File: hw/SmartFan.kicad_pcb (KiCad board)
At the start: 2 copper layers, 111 x 62.5 mm, 40 parts, among them J1 Barrel_Jack, J2 JTAG_SWD, J3 FAN_CONN, Q1 MMBT2222A-TP, Q2 MMBT2222A-TP, Q3 MMBT2222A-TP, Q4 MMBT2222A-7-F, Q5 MMBT2222A-7-F, Q6 MMBT2222A-7-F, U1 L7805CV, U2 LTV-816S-TA1, U3 LTV-816S-TA1, U4 LTV-816S-TA1

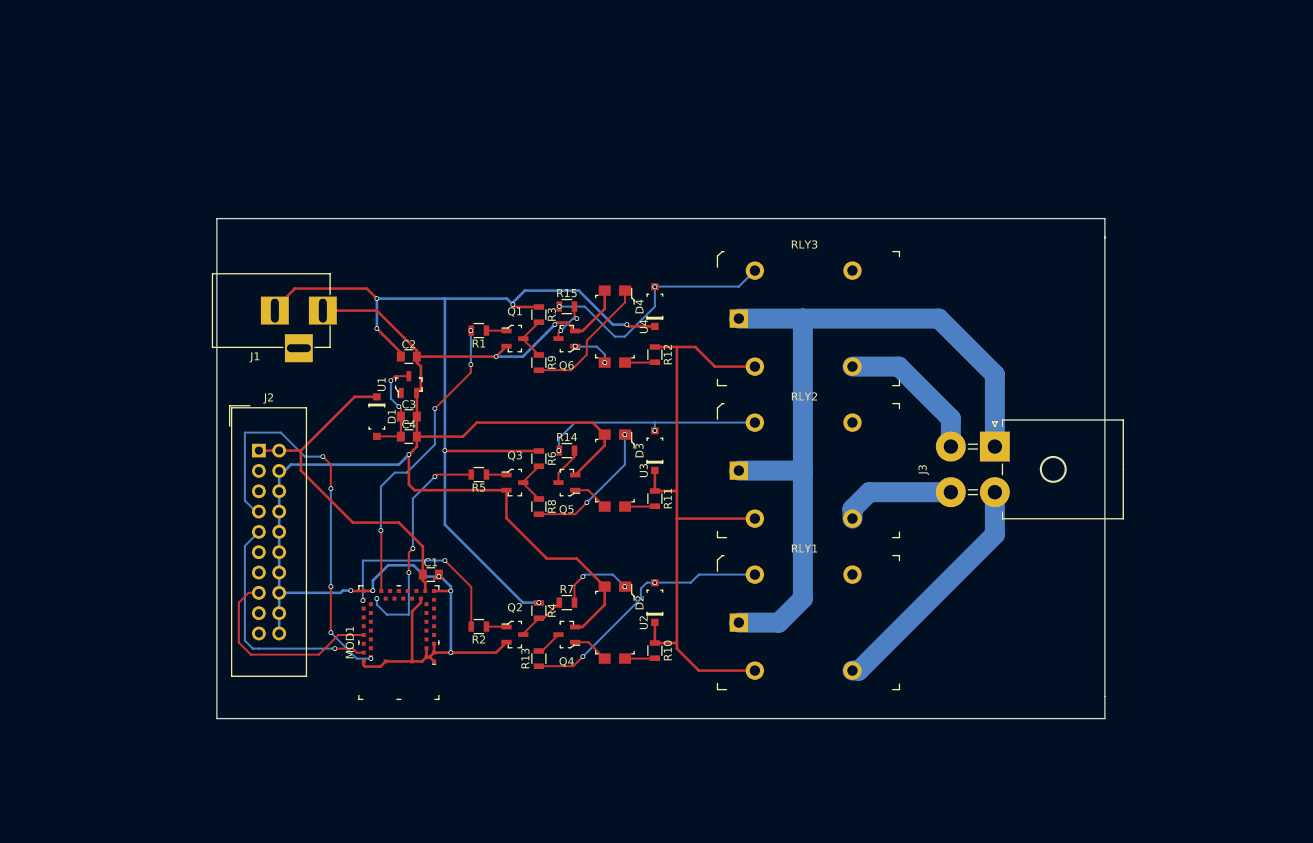
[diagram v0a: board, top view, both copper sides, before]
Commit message: Updated schematics and PCB
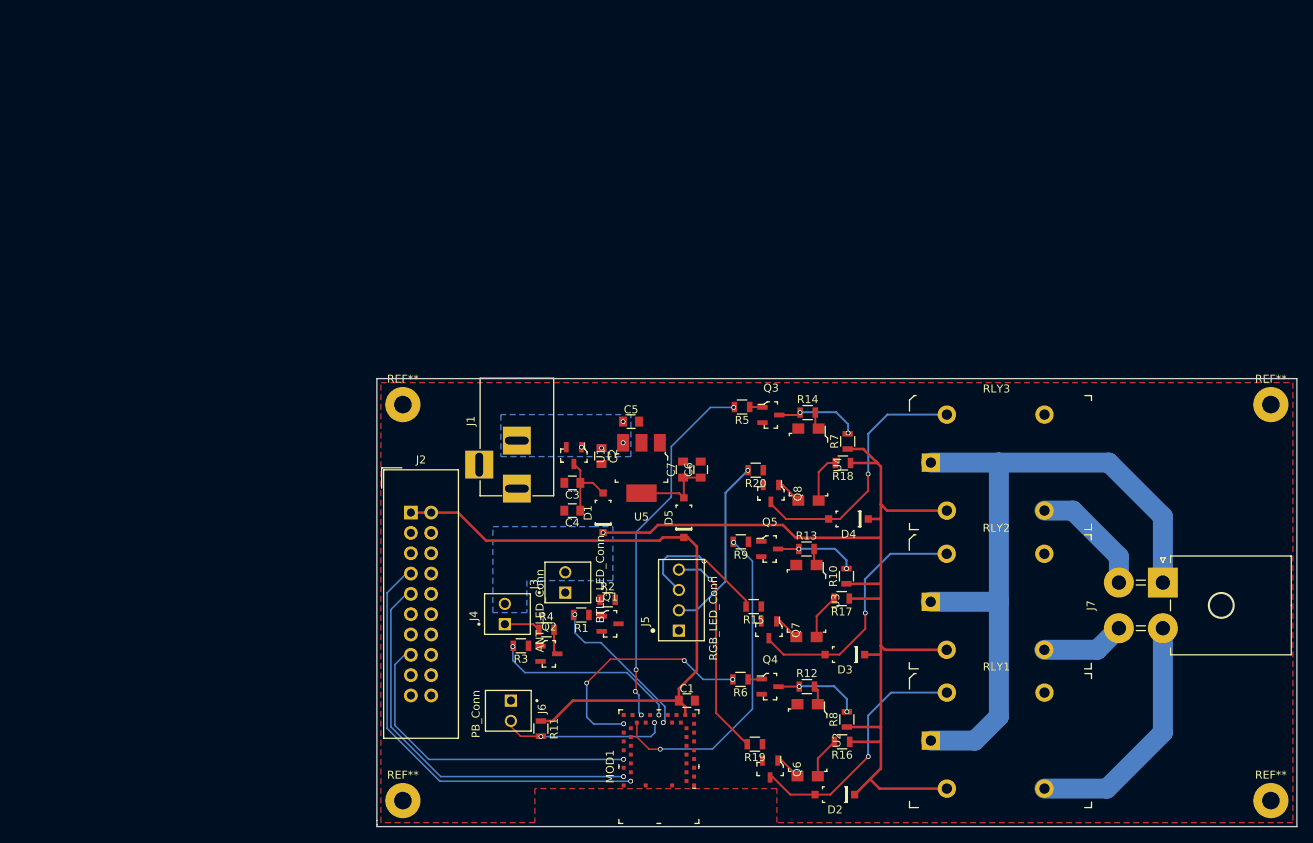
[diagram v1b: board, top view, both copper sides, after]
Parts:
- added C5: 1uF, Capacitors_SMD:C_0805, F.Cu at (143.8, 85.4)
- added C6: 1uF, Capacitors_SMD:C_0805, F.Cu at (152.5, 91.4)
- added C7: 0.1uF, Capacitors_SMD:C_0805, F.Cu at (150.3, 91.4)
- added D5: MBR0540T1G, digikey-footprints:SOD-123, F.Cu at (150.4, 97.4)
- added J4: ANT_LED_Conn, 640456-2:TE_640456-2, F.Cu at (128.0, 110.7)
- added J5: RGB_LED_Conn, 640456-4:TE_640456-4, F.Cu at (149.8, 111.5)
- added J6: PB_Conn, 640456-2:TE_640456-2, F.Cu at (128.8, 120.2)
- added J7: FAN_CONN, Connectors_Molex:Molex_MegaFit_2x02x5.70mm_Angled, F.Cu at (210.2, 105.5)
- added Q7: MMBT2222A-7-F, digikey-footprints:SOT-23-3, F.Cu at (161.0, 111.4)
- added Q8: MMBT2222A-7-F, digikey-footprints:SOT-23-3, F.Cu at (161.2, 94.3)
- added R16: 1k, Resistors_SMD:R_0805, F.Cu at (170.2, 125.4)
- added R17: 1k, Resistors_SMD:R_0805, F.Cu at (170.1, 107.5)
- added R18: 1k, Resistors_SMD:R_0805, F.Cu at (170.2, 90.5)
- added R19: 330, Resistors_SMD:R_0805, F.Cu at (159.2, 125.7)
- added R20: 330, Resistors_SMD:R_0805, F.Cu at (159.3, 91.5)
- added REF**: MountingHole_2.2mm_M2_Pad, Mounting_Holes:MountingHole_2.2mm_M2_Pad, F.Cu at (115.2, 83.2)
- added REF**: MountingHole_2.2mm_M2_Pad, Mounting_Holes:MountingHole_2.2mm_M2_Pad, F.Cu at (115.2, 132.8)
- added REF**: MountingHole_2.2mm_M2_Pad, Mounting_Holes:MountingHole_2.2mm_M2_Pad, F.Cu at (223.8, 132.8)
- added REF**: MountingHole_2.2mm_M2_Pad, Mounting_Holes:MountingHole_2.2mm_M2_Pad, F.Cu at (223.8, 83.2)
- added U5: LD1117S33CTR, digikey-footprints:SOT-223, F.Cu at (145.1, 91.2)
- J3: value FAN_CONN -> BTLE_LED_Conn; footprint Connectors_Molex:Molex_MegaFit_2x02x5.70mm_Angled -> 640456-2:TE_640456-2
- Q1, Q2: value MMBT2222A-TP -> MMBT2222A-7-F
- Q4, Q5: value MMBT2222A-7-F -> MMBT2222A-TP
- R1: value 1k -> 220
- R10, R11, R7, R8: value 1k -> 10k
- R15, R2: value 1k -> 330
- R3: value 10k -> 220
- R4: value 10k -> 330
- R6: value 10k -> 1k
- moved Q6 59.5 mm to (161.2, 128.8), turned to 270 degrees
- moved J3 56.7 mm to (135.6, 106.8), turned to 90 degrees
- moved R8 46.8 mm to (170.8, 122.6), turned to 90 degrees
- moved R12 45.6 mm to (165.8, 118.5), turned to 0 degrees
- moved R15 44.2 mm to (159.1, 108.5), turned to 180 degrees
- moved R3 41.5 mm to (130.0, 113.4), turned to 180 degrees
- moved R7 40.5 mm to (170.8, 87.8), turned to 90 degrees
- moved R1 37.8 mm to (137.6, 109.5)
- moved Q1 37.6 mm to (141.2, 110.7)
- moved R6 37.4 mm to (157.4, 117.6), turned to 180 degrees
- moved R13 36.1 mm to (165.7, 101.3), turned to 0 degrees
- moved MOD1 36.0 mm to (147.2, 128.5)
- moved D4 35.9 mm to (170.9, 97.5), turned to 180 degrees
- moved C1 35.7 mm to (150.8, 120.2)
- moved D3 34.8 mm to (170.5, 114.5), turned to 180 degrees
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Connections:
- C2 pad 1: +5V -> +9V
- D1 pad K: +3V3 -> +5V
- J1 pad 2: +5V -> +9V
- J3 pad 1: /120VAC_IN -> Net-(J3-Pad1)
- J3 pad 2: /LO_SPD_120VAC -> +5V
- MOD1 pad 22: Net-(MOD1-Pad22) -> /BTLE_LED
- MOD1 pad 23: Net-(MOD1-Pad23) -> /ANT_LED
- MOD1 pad 24: Net-(MOD1-Pad24) -> /SPD_CTRL_PB
- Q1 pad 3: /HI_SPD_EN -> Net-(Q1-Pad3)
- Q2 pad 3: /LO_SPD_EN -> Net-(Q2-Pad3)
- Q3 pad 3: /MED_SPD_EN -> /HI_SPD_EN
- Q4 pad 3: Net-(Q4-Pad3) -> /LO_SPD_EN
- Q5 pad 3: Net-(Q5-Pad3) -> /MED_SPD_EN
- Q6 pad 3: Net-(Q6-Pad3) -> Net-(D2-PadA)
- R1 pad 2: Net-(MOD1-Pad27) -> /BTLE_LED
- R10 pad 2: Net-(R10-Pad2) -> /MED_SPD_EN
- R11 pad 1: +5V -> +3V3
- R11 pad 2: Net-(R11-Pad2) -> /SPD_CTRL_PB
- R12 pad 1: +5V -> /LO_SPD_EN
- R13 pad 1: Net-(D2-PadA) -> /MED_SPD_EN
- R13 pad 2: Net-(Q4-Pad3) -> Net-(R13-Pad2)
- R14 pad 1: Net-(D3-PadA) -> /HI_SPD_EN
- R14 pad 2: Net-(Q5-Pad3) -> Net-(R14-Pad2)
- R15 pad 1: Net-(D4-PadA) -> GND
- R15 pad 2: Net-(Q6-Pad3) -> /RGB_LED_Y
- R2 pad 1: Net-(Q2-Pad1) -> Net-(J3-Pad1)
- R2 pad 2: Net-(MOD1-Pad31) -> Net-(Q1-Pad3)
- R3 pad 1: +5V -> Net-(Q2-Pad1)
- R3 pad 2: /HI_SPD_EN -> /ANT_LED
- R4 pad 1: +5V -> Net-(J4-Pad1)
- R4 pad 2: /LO_SPD_EN -> Net-(Q2-Pad3)
- R5 pad 2: Net-(MOD1-Pad28) -> Net-(MOD1-Pad27)
- R6 pad 1: +5V -> Net-(Q4-Pad1)
- R6 pad 2: /MED_SPD_EN -> Net-(MOD1-Pad31)
- R7 pad 1: /LO_SPD_EN -> +5V
- R7 pad 2: Net-(R7-Pad2) -> /HI_SPD_EN
- R8 pad 1: /MED_SPD_EN -> +5V
- R8 pad 2: Net-(R8-Pad2) -> /LO_SPD_EN
- R9 pad 1: /HI_SPD_EN -> Net-(Q5-Pad1)
- R9 pad 2: Net-(R9-Pad2) -> Net-(MOD1-Pad28)
- U1 pad 1: +5V -> +9V
- U2 pad 1: Net-(R7-Pad2) -> Net-(R12-Pad2)
- U2 pad 3: Net-(Q4-Pad1) -> Net-(Q6-Pad1)
- U2 pad 4: Net-(R10-Pad2) -> Net-(R16-Pad2)
- U3 pad 1: Net-(R8-Pad2) -> Net-(R13-Pad2)
- U3 pad 3: Net-(Q5-Pad1) -> Net-(Q7-Pad1)
- U3 pad 4: Net-(R11-Pad2) -> Net-(R17-Pad2)
- U4 pad 1: Net-(R9-Pad2) -> Net-(R14-Pad2)
- U4 pad 3: Net-(Q6-Pad1) -> Net-(Q8-Pad1)
- U4 pad 4: Net-(R12-Pad2) -> Net-(R18-Pad2)
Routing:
- net GND: track 237.3 -> 0.00 mm, vias 8 -> 0
- net +5V: track 202.7 -> 134.8 mm, vias 6 -> 1
- net +3V3: track 44.9 -> 78.5 mm
- net /RGB_LED_G: track 0.00 -> 26.9 mm, vias 0 -> 1
- net /ANT_LED: track 0.00 -> 23.7 mm, vias 0 -> 2
- net /RGB_LED_R: track 0.00 -> 22.4 mm, vias 0 -> 1
- net /SPD_CTRL_PB: track 0.00 -> 20.7 mm, vias 0 -> 2
- net /SWCLK: track 29.8 -> 49.6 mm
- net /BTLE_LED: track 0.00 -> 19.6 mm, vias 0 -> 2
- net /RGB_LED_Y: track 0.00 -> 18.2 mm, vias 0 -> 1
- net Net-(R8-Pad2): track 17.1 -> 0.00 mm, vias 2 -> 0
- net Net-(R9-Pad2): track 16.8 -> 0.00 mm
- net /~RESET: track 25.2 -> 40.5 mm, vias 0 -> 1
- net Net-(MOD1-Pad28): track 28.5 -> 40.9 mm, vias 4 -> 2
- net Net-(C6-Pad1): track 0.00 -> 10.3 mm
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- added copper zone on B.Cu, net +5V
- added copper zone on B.Cu, net +9V
- added copper zone on F.Cu, net GND
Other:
- board size 111 x 62.5 mm -> 115 x 56 mm

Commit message: Updates to PCB layout
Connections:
- REF** pad 1: (no net) -> GND (x4)
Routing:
- net GND: track 0.00 -> 7.32 mm
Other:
- board text added: "SmartFan Controller"
- board text added: "Version 1.0 Rev. 0"
- board text added: "http://www.chaoticfocus.net"
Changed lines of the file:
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@@
 (kicad_pcb (version 4) (host pcbnew 4.0.7-e2-6376~61~ubuntu18.04.1)
   (general
-    (links 124)
-    (no_connects 8)
+    (links 128)
+    (no_connects 5)
     (area 111.924999 79.924999 227.075001 136.075001)
     (thickness 1.6)
-    (drawings 7)
-    (tracks 302)
+    (drawings 10)
+    (tracks 313)
     (zones 0)
     (modules 60)
@@
     (tags "mounting hole 2.2mm m2")
     (attr virtual)
-    (fp_text reference REF** (at 0 -3.2) (layer F.SilkS)
+    (fp_text reference REF** (at 0 -3.2) (layer F.SilkS) hide
       (effects (font (size 1 1) (thickness 0.15)))
     )
@@
     (fp_circle (center 0 0) (end 2.2 0) (layer Cmts.User) (width 0.15))
     (fp_circle (center 0 0) (end 2.45 0) (layer F.CrtYd) (width 0.05))
-    (pad 1 thru_hole circle (at 0 0) (size 4.4 4.4) (drill 2.2) (layers *.Cu *.Mask))
+    (pad 1 thru_hole circle (at 0 0) (size 4.4 4.4) (drill 2.2) (layers *.Cu *.Mask)
+      (net 2 GND))
   )
   (module Mounting_Holes:MountingHole_2.2mm_M2_Pad (layer F.Cu)
@@
     (tags "mounting hole 2.2mm m2")
     (attr virtual)
-    (fp_text reference REF** (at 0 -3.2) (layer F.SilkS)
+    (fp_text reference REF** (at 0 -3.2) (layer F.SilkS) hide
       (effects (font (size 1 1) (thickness 0.15)))
     )
@@
       (effects (font (size 1 1) (thickness 0.15)))
     )
-    (fp_text user %R (at 0.3 0) (layer F.Fab)
+    (fp_text user %R (at 0.3 0) (layer F.Fab) hide
       (effects (font (size 1 1) (thickness 0.15)))
     )
     (fp_circle (center 0 0) (end 2.2 0) (layer Cmts.User) (width 0.15))
     (fp_circle (center 0 0) (end 2.45 0) (layer F.CrtYd) (width 0.05))
-    (pad 1 thru_hole circle (at 0 0) (size 4.4 4.4) (drill 2.2) (layers *.Cu *.Mask))
+    (pad 1 thru_hole circle (at 0 0) (size 4.4 4.4) (drill 2.2) (layers *.Cu *.Mask)
+      (net 2 GND))
   )
   (module Mounting_Holes:MountingHole_2.2mm_M2_Pad (layer F.Cu)
@@
     (tags "mounting hole 2.2mm m2")
     (attr virtual)
-    (fp_text reference REF** (at 0 -3.2) (layer F.SilkS)
+    (fp_text reference REF** (at 0 -3.2) (layer F.SilkS) hide
       (effects (font (size 1 1) (thickness 0.15)))
     )
@@
     (fp_circle (center 0 0) (end 2.2 0) (layer Cmts.User) (width 0.15))
     (fp_circle (center 0 0) (end 2.45 0) (layer F.CrtYd) (width 0.05))
-    (pad 1 thru_hole circle (at 0 0) (size 4.4 4.4) (drill 2.2) (layers *.Cu *.Mask))
+    (pad 1 thru_hole circle (at 0 0) (size 4.4 4.4) (drill 2.2) (layers *.Cu *.Mask)
+      (net 2 GND))
   )
   (module Mounting_Holes:MountingHole_2.2mm_M2_Pad (layer F.Cu)
@@
     (tags "mounting hole 2.2mm m2")
     (attr virtual)
-    (fp_text reference REF** (at 0 -3.2) (layer F.SilkS)
+    (fp_text reference REF** (at 0 -3.2) (layer F.SilkS) hide
       (effects (font (size 1 1) (thickness 0.15)))
     )
@@
       (effects (font (size 1 1) (thickness 0.15)))
     )
-    (fp_text user %R (at 0.3 0) (layer F.Fab)
+    (fp_text user %R (at 0.3 0) (layer F.Fab) hide
       (effects (font (size 1 1) (thickness 0.15)))
     )
     (fp_circle (center 0 0) (end 2.2 0) (layer Cmts.User) (width 0.15))
     (fp_circle (center 0 0) (end 2.45 0) (layer F.CrtYd) (width 0.05))
-    (pad 1 thru_hole circle (at 0 0) (size 4.4 4.4) (drill 2.2) (layers *.Cu *.Mask))
+    (pad 1 thru_hole circle (at 0 0) (size 4.4 4.4) (drill 2.2) (layers *.Cu *.Mask)
+      (net 2 GND))
+  )
+  (gr_text http://www.chaoticfocus.net (at 210.75 81.25) (layer F.SilkS)
+    (effects (font (size 1 1) (thickness 0.25)))
+  )
+  (gr_text "Version 1.0\nRev. 0" (at 219.25 93.5 270) (layer F.SilkS)
+    (effects (font (size 1 1) (thickness 0.25)))
+  )
+  (gr_text " SmartFan \nController" (at 223.75 93.25 270) (layer F.SilkS)
+    (effects (font (size 1.5 1.5) (thickness 0.3)))
   )
   (gr_line (start 112 80) (end 226 80) (angle 90) (layer Edge.Cuts) (width 0.15))
@@
   (segment (start 152 116.5) (end 149.75 118.75) (width 0.325) (layer F.Cu) (net 1))
   (segment (start 149.75 118.75) (end 149.75 120.25) (width 0.325) (layer F.Cu) (net 1))
+  (segment (start 142.85 130.85) (end 142.925 130.85) (width 0.325) (layer F.Cu) (net 2))
+  (segment (start 142.925 130.85) (end 143.1 131.025) (width 0.325) (layer F.Cu) (net 2))
+  (segment (start 143.1 131.025) (end 145.425 131.025) (width 0.325) (layer F.Cu) (net 2))
+  (segment (start 145.425 131.025) (end 145.6 130.85) (width 0.325) (layer F.Cu) (net 2))
+  (segment (start 151.65 122.05) (end 151.65 122.1) (width 0.325) (layer F.Cu) (net 2))
+  (segment (start 151.65 122.1) (end 150.75 123) (width 0.325) (layer F.Cu) (net 2))
+  (segment (start 150.75 123) (end 150 123) (width 0.325) (layer F.Cu) (net 2))
+  (segment (start 150.7 130.3) (end 151.1 130.3) (width 0.325) (layer F.Cu) (net 2))
+  (segment (start 151.1 130.3) (end 151.65 129.75) (width 0.325) (layer F.Cu) (net 2))
+  (segment (start 150.7 129.2) (end 151.1 129.2) (width 0.325) (layer F.Cu) (net 2))
+  (segment (start 151.1 129.2) (end 151.65 128.65) (width 0.325) (layer F.Cu) (net 2))
   (segment (start 140.275 99.25) (end 146.175 99.25) (width 0.325) (layer F.Cu) (net 3))
   (segment (start 164.35 99.9) (end 175 99.9) (width 0.325) (layer F.Cu) (net 3))
@@
     )
   )
-  (zone (net 2) (net_name GND) (layer F.Cu) (hatch edge 0.508)
-    (connect_pads (clearance 0.508))
-    (min_thickness 0.254)
-    (fill yes (arc_segments 16) (thermal_gap 0.508) (thermal_bridge_width 0.508))
-    (polygon
-      (pts
-        (xy 226.5 135.5) (xy 162 135.5) (xy 162 131.25) (xy 131.75 131.25) (xy 131.75 135.5)
-        (xy 112.5 135.5) (xy 112.5 80.5) (xy 226.5 80.5)
-      )
-    )
-  )
   (zone (net 64) (net_name +9V) (layer B.Cu) (hatch edge 0.508)
     (connect_pads (clearance 0.508))
@@
       )
     )
+  )
+  (zone (net 2) (net_name GND) (layer F.Cu) (hatch edge 0.508)
+    (connect_pads (clearance 0.508))
+    (min_thickness 0.254)
+    (fill yes (arc_segments 16) (thermal_gap 0.508) (thermal_bridge_width 0.508))
+    (polygon
+      (pts
+        (xy 226.75 80.25) (xy 226.75 135.75) (xy 161.75 135.75) (xy 161.75 131.25) (xy 132 131.25)
+        (xy 132 135.75) (xy 112.25 135.75) (xy 112.25 80.25) (xy 176.75 80.25)
+      )
+    )
+    (polygon
+      (pts        (xy 220.5 135) (xy 220.5 82) (xy 176.75 82) (xy 176.75 135)
+      )
+    )
